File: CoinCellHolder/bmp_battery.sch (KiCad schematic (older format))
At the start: 8 parts, among them P1 Conn_01x01_Female, P2 Conn_01x01_Female

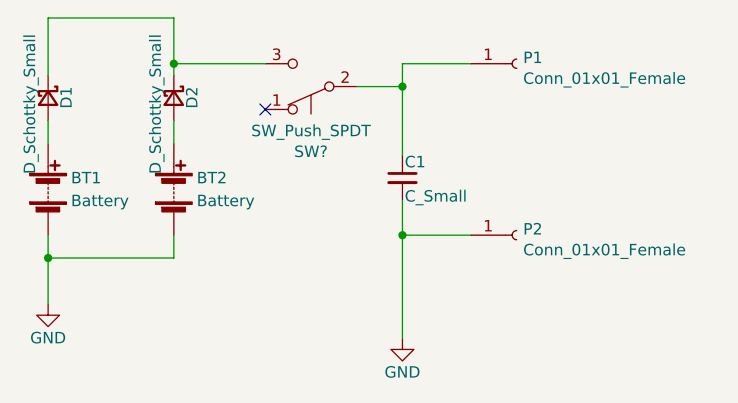
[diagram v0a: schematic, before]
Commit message: SW1をつけた
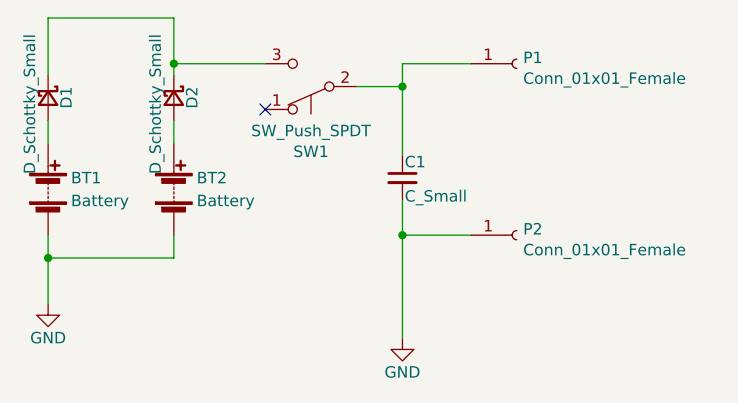
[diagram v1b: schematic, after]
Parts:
- gave numbers to parts that had none: 1
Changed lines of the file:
@@
 	6100 3900 6300 3900
 $Comp
-L Switch:SW_Push_SPDT SW?
+L Switch:SW_Push_SPDT SW1
 U 1 1 61D7B1A6
 P 5900 3900
-F 0 "SW?" H 5900 4185 50  0000 C CNN
+F 0 "SW1" H 5900 4185 50  0000 C CNN
 F 1 "SW_Push_SPDT" H 5900 4094 50  0000 C CNN
 F 2 "MyLib:MK12C02" H 5900 3900 50  0001 C CNN
